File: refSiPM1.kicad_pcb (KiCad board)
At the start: 2 copper layers, 60 x 31.8 mm, 9 parts, among them J1 U.FL-R-SMT-1_10_, J2 U.FL-R-SMT-1_10_, J3 U.FL-R-SMT-1_10_, J4 U.FL-R-SMT-1_10_, J5 U.FL-R-SMT-1_10_, J6 U.FL-R-SMT-1_10_, J7 U.FL-R-SMT-1_10_, J8 U.FL-R-SMT-1_10_

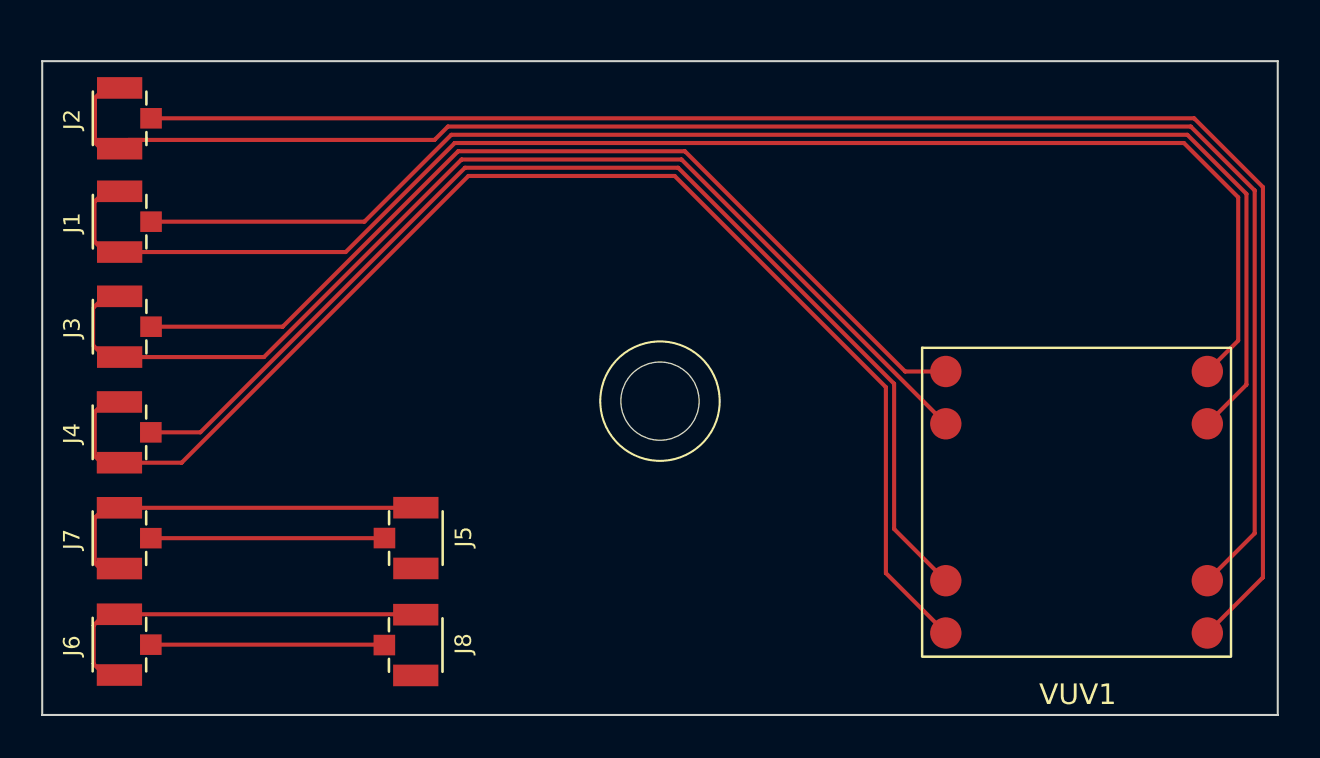
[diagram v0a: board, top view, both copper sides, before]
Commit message: adjusted traces and added silkscreen
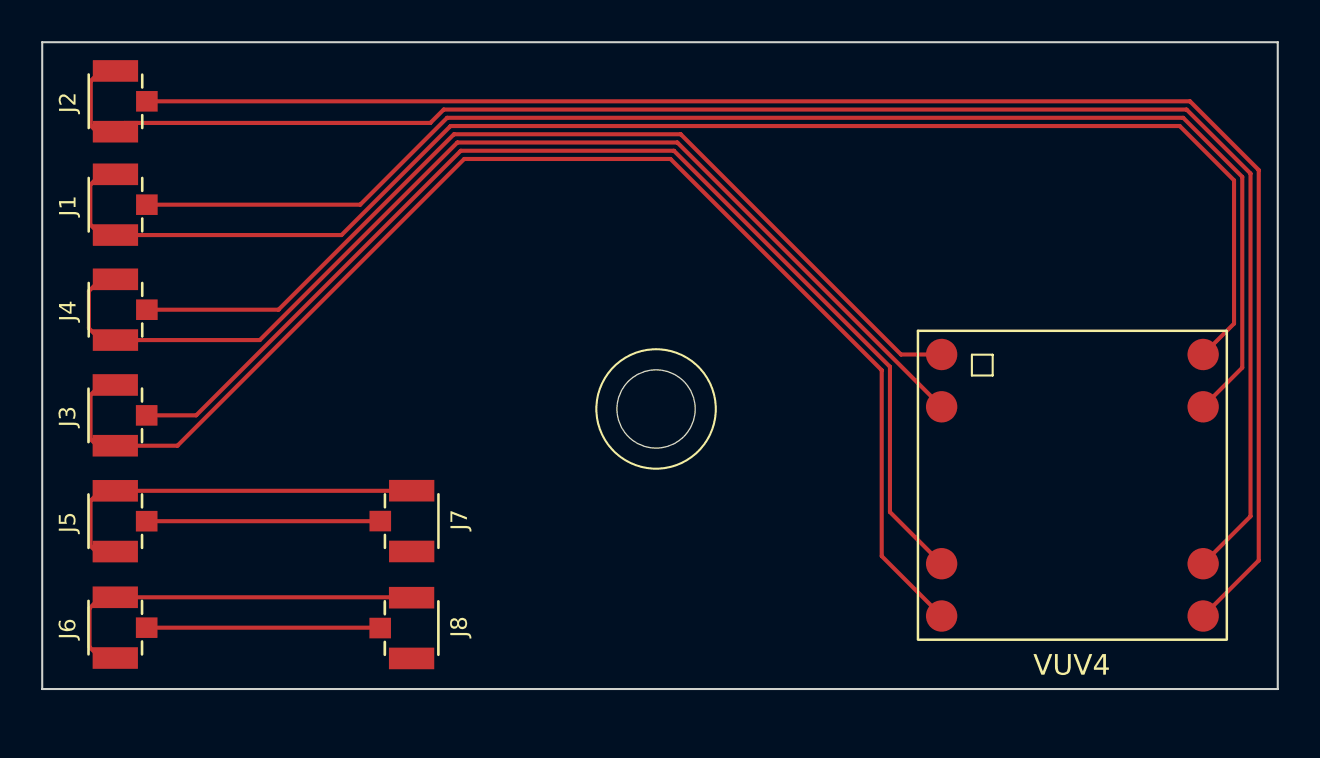
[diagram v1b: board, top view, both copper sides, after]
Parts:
- moved J1 0.85 mm to (120.2, 69.9)
- moved J4 0.85 mm to (120.2, 75.0)
- moved J7 0.85 mm to (134.6, 85.3)
- moved J8 0.85 mm to (134.6, 90.5)
- moved VUV4 0.85 mm to (166.7, 83.5)
- moved J2 0.85 mm to (120.2, 64.9)
- moved J3 0.85 mm to (120.2, 80.1)
- moved J5 0.85 mm to (120.2, 85.3)
- moved J6 0.85 mm to (120.2, 90.4)
- renumbered J4 to J3, J3 to J4, J7 to J5, J5 to J7, VUV1 to VUV4
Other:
- board size 60 x 31.8 mm -> 60 x 31.4 mm
- board text added: "refSiPM1 Lucas Darroch Brunner Neutrino Lab"
